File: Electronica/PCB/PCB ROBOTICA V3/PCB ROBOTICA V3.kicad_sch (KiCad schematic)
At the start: 13 parts, among them J1 Ultrasonico 1, J2 Screw_Terminal_01x02, J3 Ultrasonico 2, J4 Ultrasonico 3, J5 Conn_02x05_Counter_Clockwise, J6 Screw_Terminal_01x02

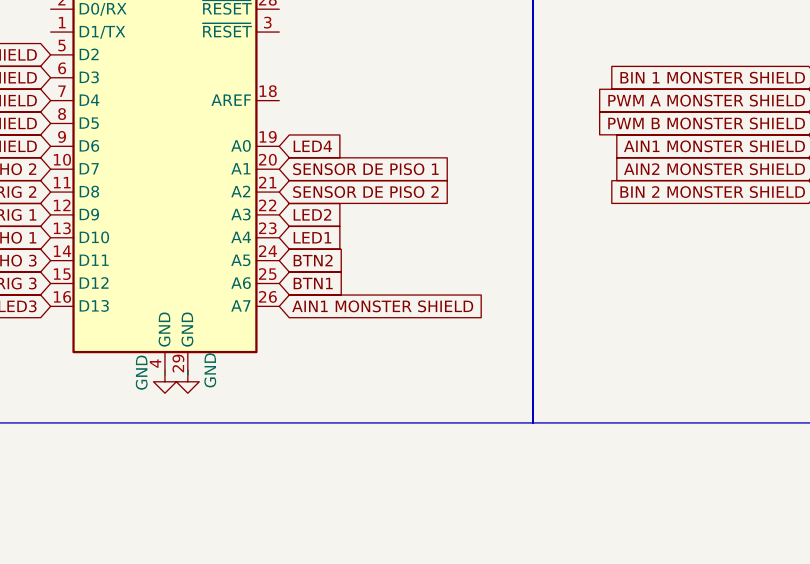
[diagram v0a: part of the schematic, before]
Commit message: Motores funcionando, no funciona con ultrasonicos
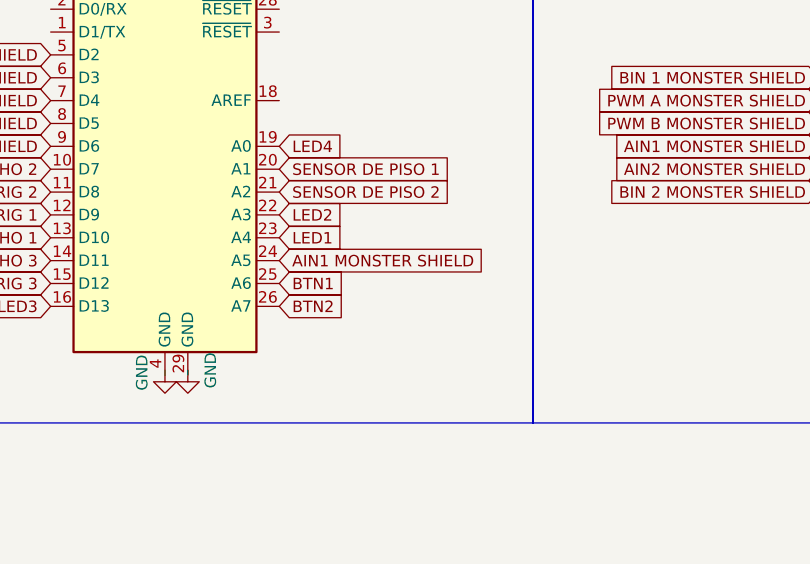
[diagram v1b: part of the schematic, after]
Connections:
- net AIN1 MONSTER SHIELD: now also A1.24 (A5); no longer A1.26 (A7)
- net BTN2: now also A1.26 (A7); no longer A1.24 (A5)
